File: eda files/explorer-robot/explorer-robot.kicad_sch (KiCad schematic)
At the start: 0 parts

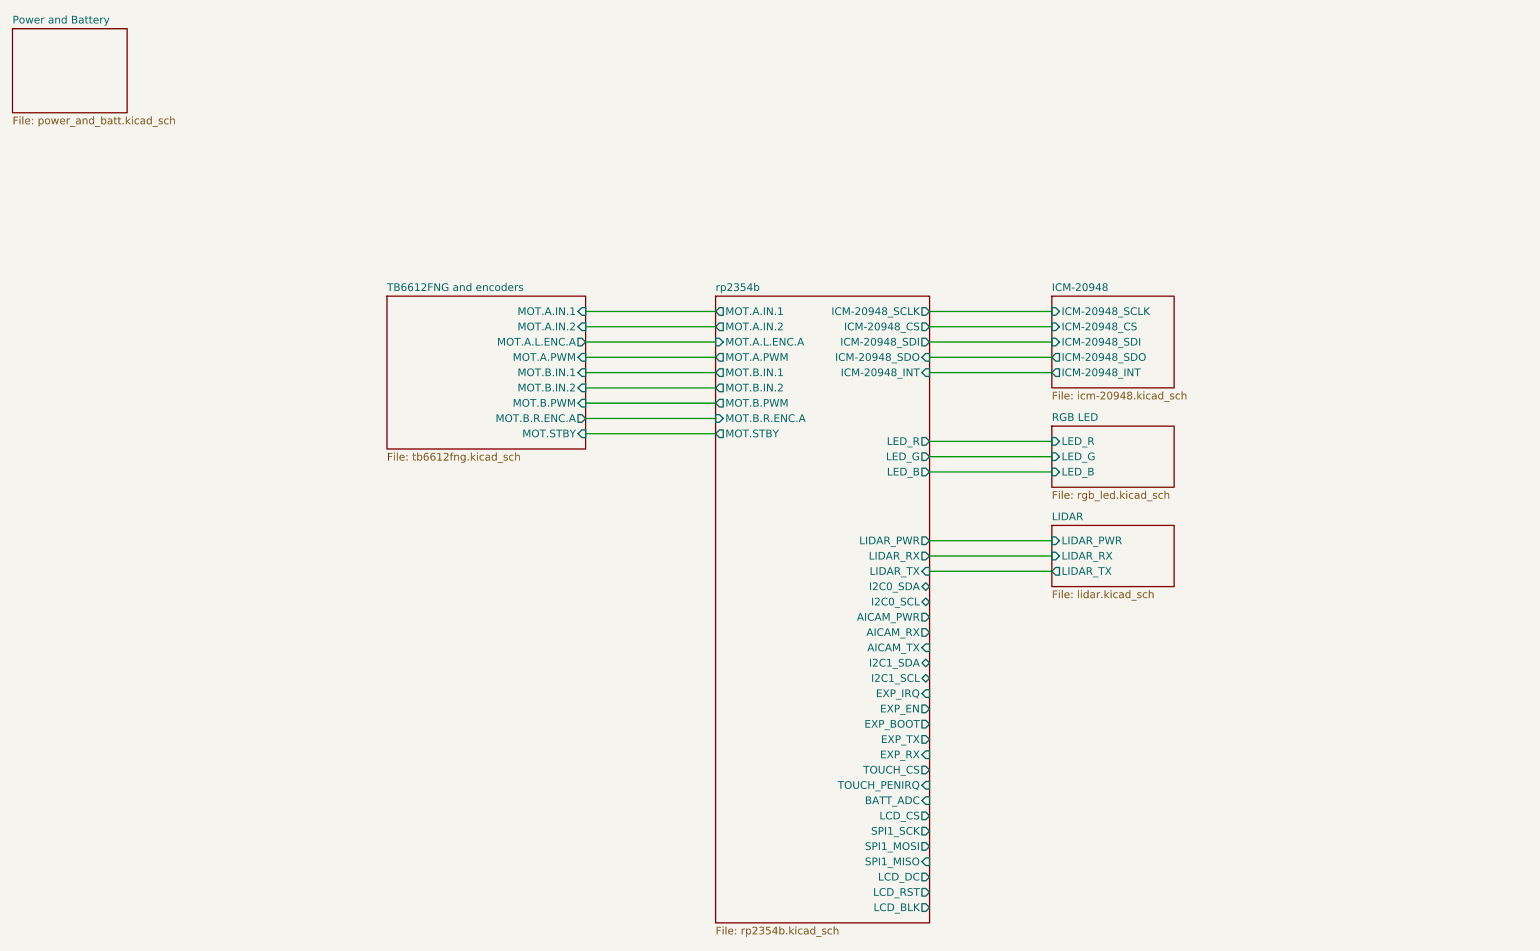
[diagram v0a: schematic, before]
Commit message: Add BATT_ADC hierarchical output to power sheet
Relocate the power/battery sheet in the schematic and expose the
battery voltage divider as a hierarchical label so it can be consumed
by the MCU.
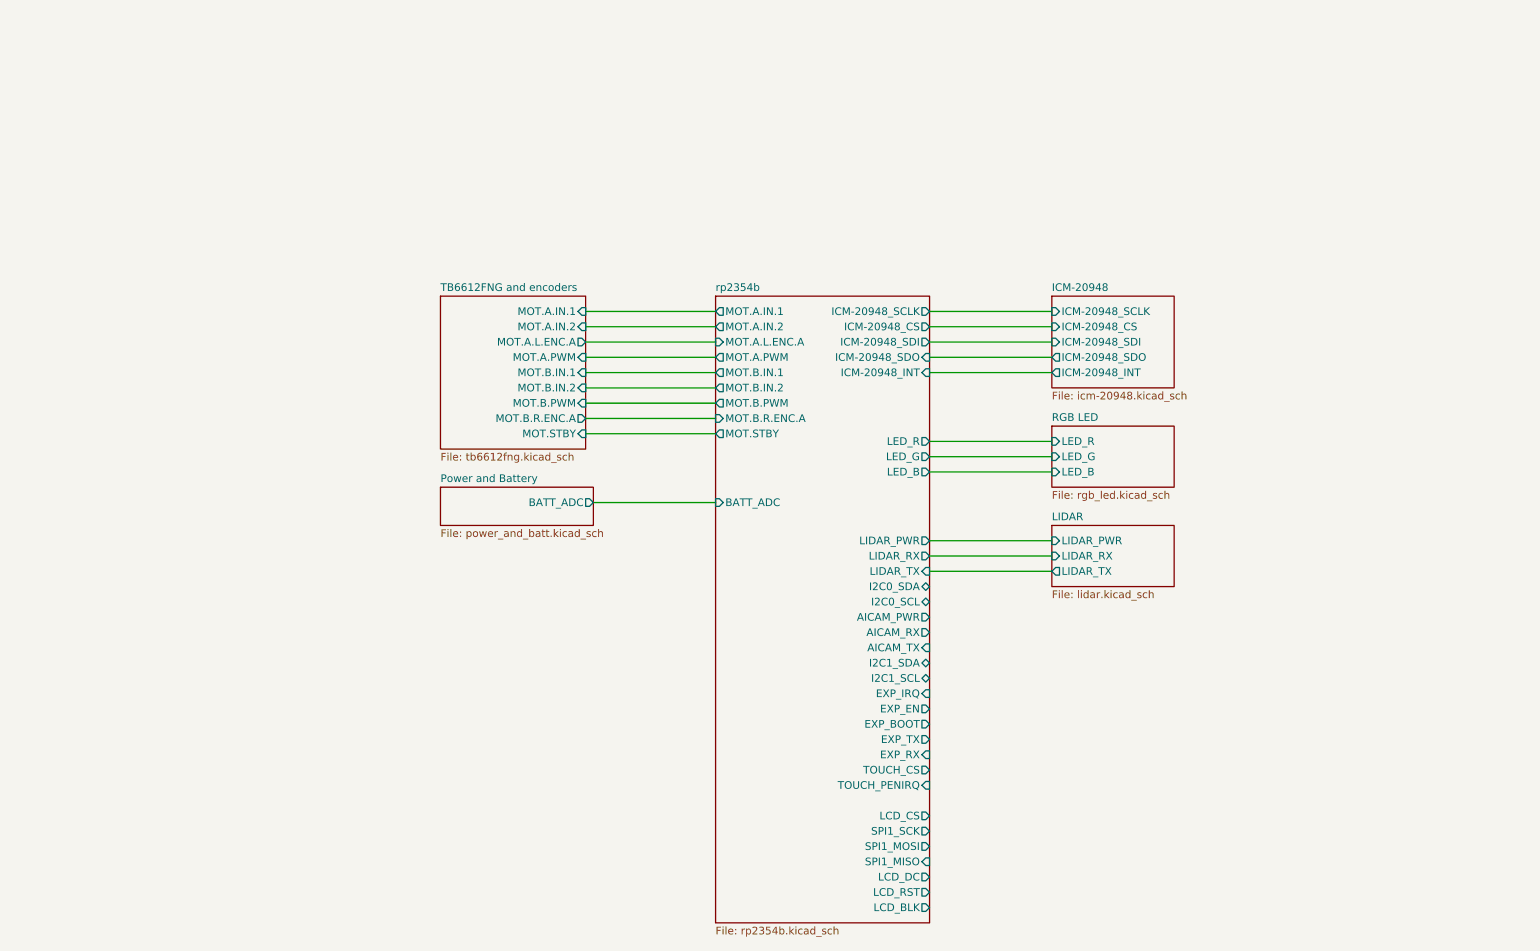
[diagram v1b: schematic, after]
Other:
- sheet Power and Battery ports: added BATT_ADC; removed none
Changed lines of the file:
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@@
+	(wire
+		(pts
+			(xy 116.84 99.06) (xy 137.16 99.06)
+		)
+		(stroke
+			(width 0)
+			(type default)
+		)
+	)
 	(wire
 		(pts
@@
 		)
 		(pin "BATT_ADC" input
-			(at 172.72 148.59 0)
-			(effects
-				(font
-					(size 1.27 1.27)
-				)
-				(justify right)
+			(at 137.16 99.06 180)
+			(effects
+				(font
+					(size 1.27 1.27)
+				)
+				(justify left)
 			)
 		)
@@
 	)
 	(sheet
-		(at 82.55 64.77)
-		(size 33.02 25.4)
+		(at 91.44 64.77)
+		(size 24.13 25.4)
 		(exclude_from_sim no)
 		(in_bom yes)
@@
 		)
 		(property "Sheetname" "TB6612FNG and encoders"
-			(at 82.55 64.0584 0)
+			(at 91.44 64.0584 0)
 			(show_name no)
 			(do_not_autoplace no)
@@
 		)
 		(property "Sheetfile" "tb6612fng.kicad_sch"
-			(at 82.55 90.7546 0)
+			(at 91.44 90.7546 0)
 			(show_name no)
 			(do_not_autoplace no)
@@
 	)
 	(sheet
-		(at 20.32 20.32)
-		(size 19.05 13.97)
+		(at 91.44 96.52)
+		(size 25.4 6.35)
 		(exclude_from_sim no)
 		(in_bom yes)
@@
 		)
 		(property "Sheetname" "Power and Battery"
-			(at 20.32 19.6084 0)
+			(at 91.44 95.8084 0)
 			(show_name no)
 			(do_not_autoplace no)
@@
 		)
 		(property "Sheetfile" "power_and_batt.kicad_sch"
-			(at 20.32 34.8746 0)
+			(at 91.44 103.4546 0)
 			(show_name no)
 			(do_not_autoplace no)
@@
 			)
 		)
+		(pin "BATT_ADC" output
+			(at 116.84 99.06 0)
+			(effects
+				(font
+					(size 1.27 1.27)
+				)
+				(justify right)
+			)
+		)

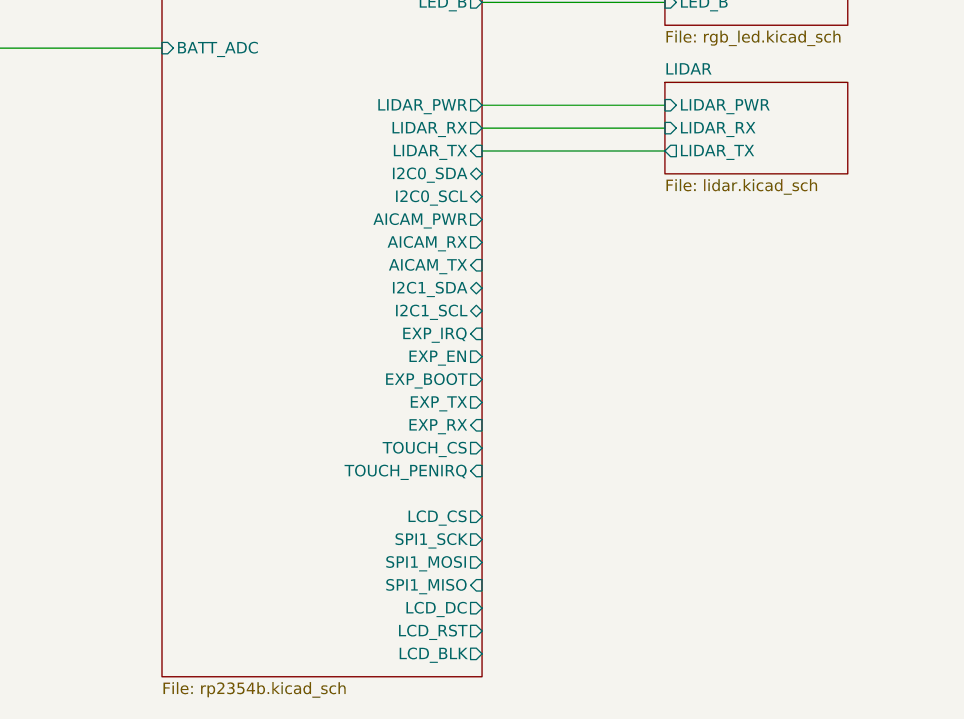
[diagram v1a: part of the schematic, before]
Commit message: Add AI CAM power switch and connector circuit
Adds a load switch, decoupling, UART series resistors, and JST
connector for the AI camera module, exposed via hierarchical
AICAM_RX/TX/PWR labels to the RP2354B.

Also drops the vendor name from the resources doc comment.
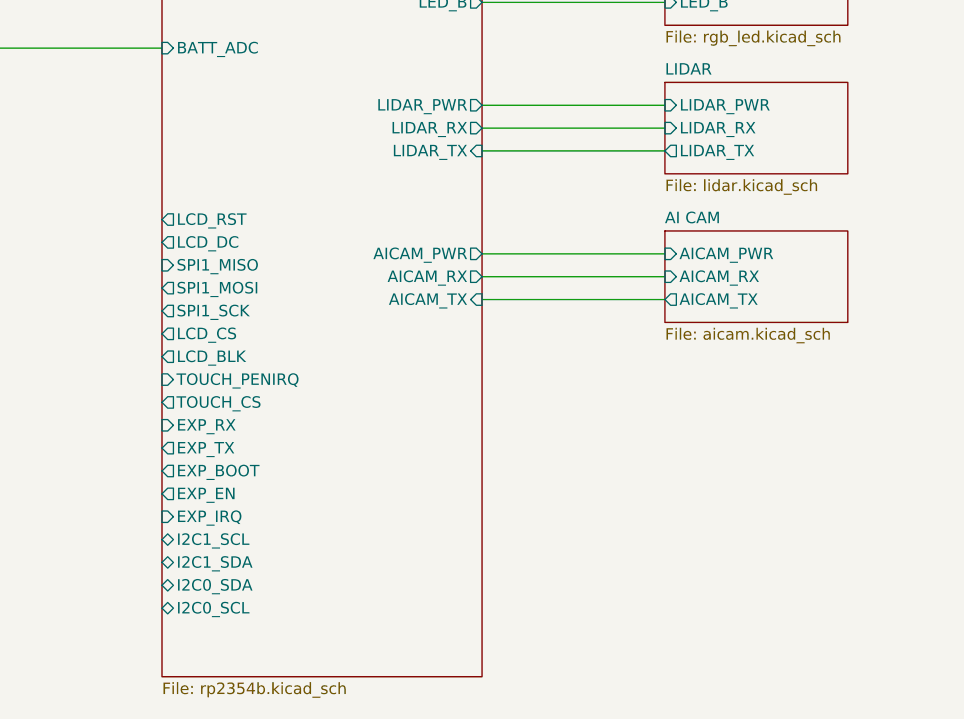
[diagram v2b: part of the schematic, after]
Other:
- added sheet AI CAM (aicam.kicad_sch)
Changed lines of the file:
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@@
+	(wire
+		(pts
+			(xy 172.72 127) (xy 193.04 127)
+		)
+		(stroke
+			(width 0)
+			(type default)
+		)
+	)
 	(wire
 		(pts
@@
 	(wire
 		(pts
+			(xy 172.72 124.46) (xy 193.04 124.46)
+		)
+		(stroke
+			(width 0)
+			(type default)
+		)
+	)
+	(wire
+		(pts
 			(xy 172.72 72.39) (xy 193.04 72.39)
 		)
@@
 		(pts
 			(xy 172.72 107.95) (xy 193.04 107.95)
+		)
+		(stroke
+			(width 0)
+			(type default)
+		)
+	)
+	(wire
+		(pts
+			(xy 172.72 121.92) (xy 193.04 121.92)
 		)
 		(stroke
@@
 		)
 		(pin "I2C0_SDA" bidirectional
-			(at 172.72 113.03 0)
-			(effects
-				(font
-					(size 1.27 1.27)
-				)
-				(justify right)
+			(at 137.16 158.75 180)
+			(effects
+				(font
+					(size 1.27 1.27)
+				)
+				(justify left)
 			)
 		)
 		(pin "I2C0_SCL" bidirectional
-			(at 172.72 115.57 0)
-			(effects
-				(font
-					(size 1.27 1.27)
-				)
-				(justify right)
+			(at 137.16 161.29 180)
+			(effects
+				(font
+					(size 1.27 1.27)
+				)
+				(justify left)
 			)
 		)
 		(pin "AICAM_PWR" output
-			(at 172.72 118.11 0)
+			(at 172.72 121.92 0)
 			(effects
 				(font
@@
 		)
 		(pin "AICAM_RX" output
-			(at 172.72 120.65 0)
+			(at 172.72 124.46 0)
 			(effects
 				(font
@@
 		)
 		(pin "AICAM_TX" input
-			(at 172.72 123.19 0)
+			(at 172.72 127 0)
 			(effects
 				(font
@@
 		)
 		(pin "I2C1_SDA" bidirectional
-			(at 172.72 125.73 0)
-			(effects
-				(font
-					(size 1.27 1.27)
-				)
-				(justify right)
+			(at 137.16 156.21 180)
+			(effects
+				(font
+					(size 1.27 1.27)
+				)
+				(justify left)
 			)
 		)
 		(pin "I2C1_SCL" bidirectional
-			(at 172.72 128.27 0)
-			(effects
-				(font
-					(size 1.27 1.27)
-				)
-				(justify right)
+			(at 137.16 153.67 180)
+			(effects
+				(font
+					(size 1.27 1.27)
+				)
+				(justify left)
 			)
 		)
 		(pin "EXP_IRQ" input
-			(at 172.72 130.81 0)
-			(effects
-				(font
-					(size 1.27 1.27)
-				)
-				(justify right)
+			(at 137.16 151.13 180)
+			(effects
+				(font
+					(size 1.27 1.27)
+				)
+				(justify left)
 			)
 		)
 		(pin "EXP_EN" output
-			(at 172.72 133.35 0)
-			(effects
-				(font
-					(size 1.27 1.27)
-				)
-				(justify right)
+			(at 137.16 148.59 180)
+			(effects
+				(font
+					(size 1.27 1.27)
+				)
+				(justify left)
 			)
 		)
 		(pin "EXP_BOOT" output
-			(at 172.72 135.89 0)
-			(effects
-				(font
-					(size 1.27 1.27)
-				)
-				(justify right)
+			(at 137.16 146.05 180)
+			(effects
+				(font
+					(size 1.27 1.27)
+				)
+				(justify left)
 			)
 		)
 		(pin "EXP_TX" output
-			(at 172.72 138.43 0)
-			(effects
-				(font
-					(size 1.27 1.27)
-				)
-				(justify right)
+			(at 137.16 143.51 180)
+			(effects
+				(font
+					(size 1.27 1.27)
+				)
+				(justify left)
 			)
 		)
 		(pin "EXP_RX" input
-			(at 172.72 140.97 0)
-			(effects
-				(font
-					(size 1.27 1.27)
-				)
-				(justify right)
+			(at 137.16 140.97 180)
+			(effects
+				(font
+					(size 1.27 1.27)
+				)
+				(justify left)
 			)
 		)
 		(pin "TOUCH_CS" output
-			(at 172.72 143.51 0)
-			(effects
-				(font
-					(size 1.27 1.27)
-				)
-				(justify right)
+			(at 137.16 138.43 180)
+			(effects
+				(font
+					(size 1.27 1.27)
+				)
+				(justify left)
 			)
 		)
 		(pin "TOUCH_PENIRQ" input
-			(at 172.72 146.05 0)
-			(effects
-				(font
-					(size 1.27 1.27)
-				)
-				(justify right)
+			(at 137.16 135.89 180)
+			(effects
+				(font
+					(size 1.27 1.27)
+				)
+				(justify left)
 			)
 		)
@@
 		)
 		(pin "LCD_CS" output
-			(at 172.72 151.13 0)
-			(effects
-				(font
-					(size 1.27 1.27)
-				)
-				(justify right)
+			(at 137.16 130.81 180)
+			(effects
+				(font
+					(size 1.27 1.27)
+				)
+				(justify left)
 			)
 		)
 		(pin "SPI1_SCK" output
-			(at 172.72 153.67 0)
-			(effects
-				(font
-					(size 1.27 1.27)
-				)
-				(justify right)
+			(at 137.16 128.27 180)
+			(effects
+				(font
+					(size 1.27 1.27)
+				)
+				(justify left)
 			)
 		)
 		(pin "SPI1_MOSI" output
-			(at 172.72 156.21 0)
-			(effects
-				(font
-					(size 1.27 1.27)
-				)
-				(justify right)
+			(at 137.16 125.73 180)
+			(effects
+				(font
+					(size 1.27 1.27)
+				)
+				(justify left)
 			)
 		)
 		(pin "SPI1_MISO" input
-			(at 172.72 158.75 0)
-			(effects
-				(font
-					(size 1.27 1.27)
-				)
-				(justify right)
+			(at 137.16 123.19 180)
+			(effects
+				(font
+					(size 1.27 1.27)
+				)
+				(justify left)
 			)
 		)
 		(pin "LCD_DC" output
-			(at 172.72 161.29 0)
-			(effects
-				(font
-					(size 1.27 1.27)
-				)
-				(justify right)
+			(at 137.16 120.65 180)
+			(effects
+				(font
+					(size 1.27 1.27)
+				)
+				(justify left)
 			)
 		)
 		(pin "LCD_RST" output
-			(at 172.72 163.83 0)
-			(effects
-				(font
-					(size 1.27 1.27)
-				)
-				(justify right)
+			(at 137.16 118.11 180)
+			(effects
+				(font
+					(size 1.27 1.27)
+				)
+				(justify left)
 			)
 		)
 		(pin "LCD_BLK" output
-			(at 172.72 166.37 0)
-			(effects
-				(font
-					(size 1.27 1.27)
-				)
-				(justify right)
+			(at 137.16 133.35 180)
+			(effects
+				(font
+					(size 1.27 1.27)
+				)
+				(justify left)
 			)
 		)
@@
 				)
 			)
+		)
+	)
+	(sheet
+		(at 193.04 119.38)
+		(size 20.32 10.16)
+		(exclude_from_sim no)
+		(in_bom yes)
+		(on_board yes)
+		(dnp no)
+		(fields_autoplaced yes)
+		(stroke
+			(width 0.1524)
+			(type solid)
+		)
+		(fill
+			(color 0 0 0 0)
+		)
+		(property "Sheetname" "AI CAM"
+			(at 193.04 118.6684 0)
+			(show_name no)
+			(do_not_autoplace no)
+			(effects
+				(font
+					(size 1.27 1.27)
+				)
+				(justify left bottom)
+			)
+		)
+		(property "Sheetfile" "aicam.kicad_sch"
+			(at 193.04 130.1246 0)
+			(show_name no)
+			(do_not_autoplace no)
+			(effects
+				(font
+					(size 1.27 1.27)
+				)
+				(justify left top)
+			)
+		)
+		(pin "AICAM_PWR" input
+			(at 193.04 121.92 180)
+			(effects
+				(font
+					(size 1.27 1.27)
+				)
+				(justify left)
+			)
+		)
+		(pin "AICAM_RX" input
+			(at 193.04 124.46 180)
+			(effects
+				(font
+					(size 1.27 1.27)
+				)
+				(justify left)
+			)
+		)
+		(pin "AICAM_TX" output
+			(at 193.04 127 180)
+			(effects
+				(font
+					(size 1.27 1.27)
+				)
+				(justify left)
+			)
+		)
+		(instances
+			(project "explorer-robot"
+				(path "/57778957-dc0c-4e39-b470-8f64ada5e845"
+					(page "8")
+				)
+			)
